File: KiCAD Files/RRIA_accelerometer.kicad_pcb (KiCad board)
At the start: 2 copper layers, 22 x 31.5 mm, 15 parts, among them J2 SPI LIS3DH, M1 Logo_Duet3d_New, U1 LIS3DH

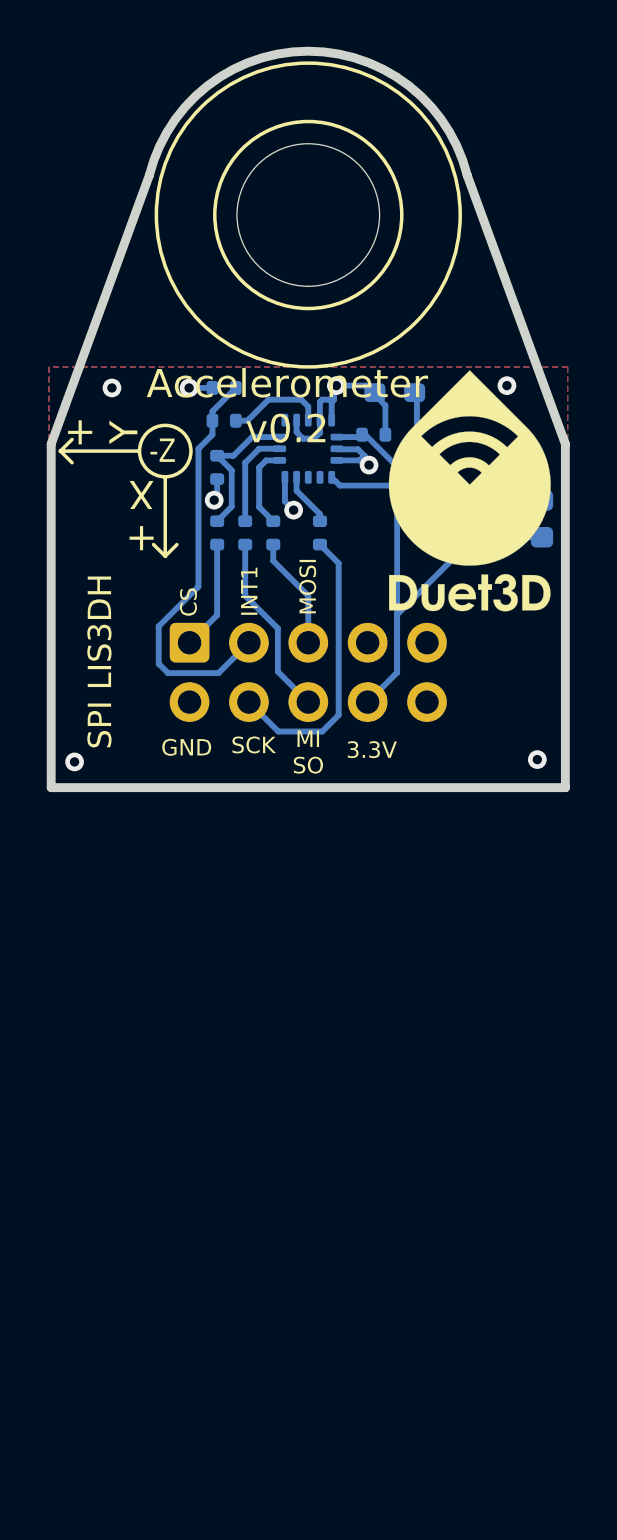
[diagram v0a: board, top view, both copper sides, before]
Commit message: gitignore + prep for RP2040
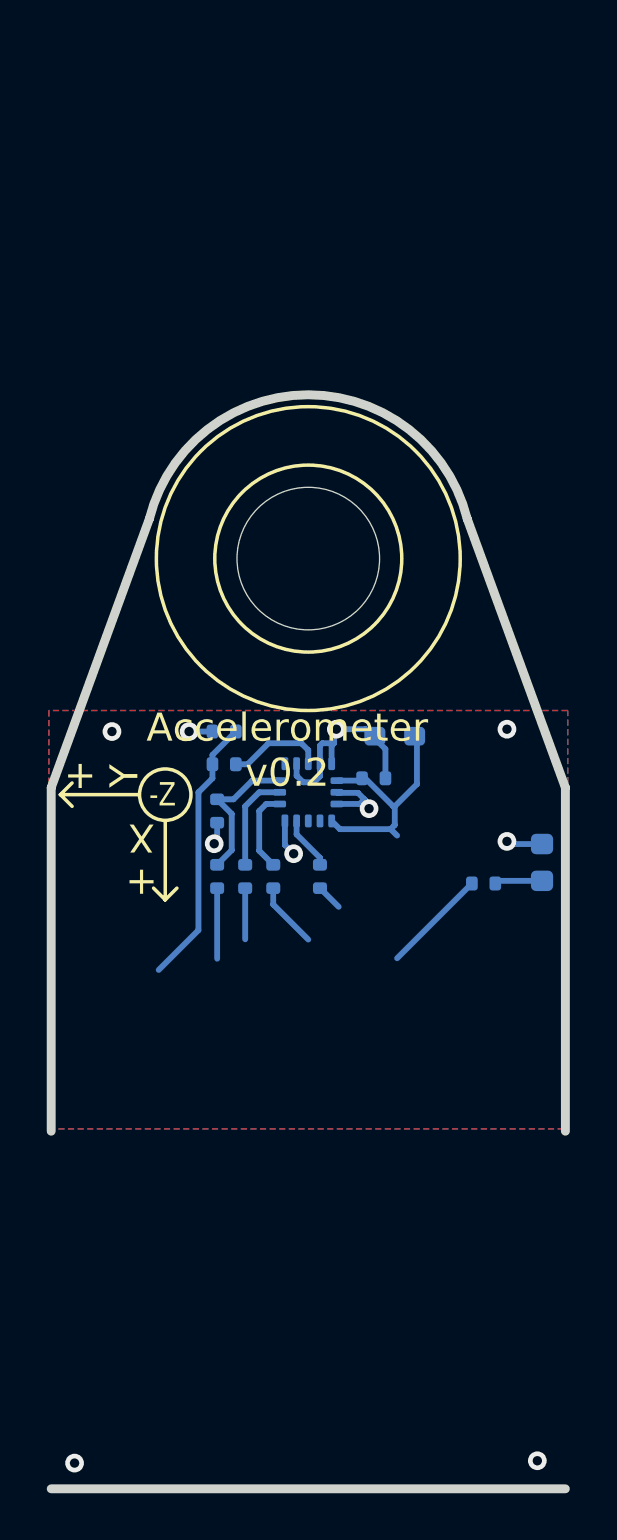
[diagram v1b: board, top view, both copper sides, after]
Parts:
- removed J2: SPI LIS3DH, Connector_IDC:IDC-Header_2x05_P2.54mm_Vertical
- removed M1: Logo_Duet3d_New, complib:LOGO_NEW_Duet3D_vertical_6mm_no_mask
- moved C1 14.7 mm to (73.8, 59.6)
- moved C3 14.7 mm to (67.1, 61.0)
- moved C4 14.7 mm to (67.4, 57.6)
- moved D1 14.7 mm to (81.0, 63.2)
- moved H1 14.7 mm to (71.0, 50.2)
- moved R1 14.7 mm to (67.4, 59.0)
- moved U1 14.7 mm to (71.0, 60.2)
- moved C2 14.7 mm to (74.7, 57.8)
- moved R2 14.7 mm to (68.3, 63.8)
- moved R3 14.7 mm to (69.5, 63.8)
- moved R4 14.7 mm to (71.5, 63.8)
- moved R5 14.7 mm to (67.1, 63.8)
- moved R6 14.7 mm to (78.5, 64.1)
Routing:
- net 3.3V: track 27.0 -> 15.0 mm
- net SPI_SCK: track 12.3 -> 1.13 mm
- net INT1: track 17.7 -> 11.6 mm
- net SPI_MISO: track 7.86 -> 2.19 mm
- net SPI_MOSI: track 4.82 -> 2.82 mm
- net SPI_CS: track 4.69 -> 3.02 mm
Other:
- board size 22 x 31.5 mm -> 22 x 46.8 mm
- board text removed: "3.3V"
- board text removed: "CS"
- board text removed: "GND"
- board text removed: "INT1"
- board text removed: "MI SO"
- board text removed: "MOSI"
- board text removed: "SCK"

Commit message: progress
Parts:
- removed D1: PWR, LED_SMD:LED_0603_1608Metric
- removed R1, R2, R3, R4, R5: 62R, Resistor_SMD:R_0402_1005Metric_Wbry
- removed R6: 220R, Resistor_SMD:R_0402_1005Metric_Wbry
- added C1: 100nF, Capacitor_SMD:C_0402_1005Metric, B.Cu at (163.4, 86.6)
- added C10: 100nF, Capacitor_SMD:C_0402_1005Metric, B.Cu at (161.3, 81.1)
- added C11: 1uF, Capacitor_SMD:C_0402_1005Metric, B.Cu at (177.2, 77.5)
- added C12: 1uF, Capacitor_SMD:C_0402_1005Metric, B.Cu at (169.4, 84.6)
- added C13: 10pF, Capacitor_SMD:C_0402_1005Metric, B.Cu at (162.7, 73.4)
- added C14: 10pF, Capacitor_SMD:C_0402_1005Metric, B.Cu at (166.6, 71.5)
- added C15: 100nF, Capacitor_SMD:C_0402_1005Metric, B.Cu at (165.0, 86.2)
- added C16: 100nF, Capacitor_SMD:C_0402_1005Metric, B.Cu at (169.3, 73.5)
- added C17: 8pF, Capacitor_SMD:C_0402_1005Metric, B.Cu at (145.7, 74.5)
- added C18: 8pF, Capacitor_SMD:C_0402_1005Metric, B.Cu at (146.0, 71.0)
- added C19: 100nF, Capacitor_SMD:C_0402_1005Metric, B.Cu at (150.9, 76.0)
- added C2: 100nF, Capacitor_SMD:C_0402_1005Metric, B.Cu at (161.4, 78.5)
- added C22: 1uF, Capacitor_SMD:C_0402_1005Metric, B.Cu at (150.9, 76.9)
- added C25: 100nF, Capacitor_SMD:C_0402_1005Metric, B.Cu at (132.6, 79.2)
- added C26: 100nF, Capacitor_SMD:C_0402_1005Metric, B.Cu at (132.6, 77.2)
- added C27: 1uF, Capacitor_SMD:C_0402_1005Metric, B.Cu at (132.6, 75.2)
- added C28: 1uF, Capacitor_SMD:C_0402_1005Metric, B.Cu at (132.6, 73.3)
- added C5: 100nF, Capacitor_SMD:C_0402_1005Metric, B.Cu at (168.4, 73.5)
- added C6: 1uF, Capacitor_SMD:C_0402_1005Metric, B.Cu at (168.5, 84.6)
- added C7: 100nF, Capacitor_SMD:C_0402_1005Metric, B.Cu at (171.5, 77.5)
- added C8: 100nF, Capacitor_SMD:C_0402_1005Metric, B.Cu at (165.9, 85.7)
- added C9: 100nF, Capacitor_SMD:C_0402_1005Metric, B.Cu at (166.8, 84.8)
- added J3: 2.54-Header-1x2, Connector_PinHeader_2.54mm:PinHeader_1x02_P2.54mm_Vertical, F.Cu at (185.6, 62.4)
- added R10: 1k, Resistor_SMD:R_0402_1005Metric, B.Cu at (166.6, 73.4)
- added R7: 120Ω, PCM_Resistor_SMD_AKL:R_0402_1005Metric, B.Cu at (130.7, 85.9)
- added SW1: TS-1088, Button_Switch_SMD:SW_SPST_TS-1088-xR025, B.Cu at (192.1, 62.0)
- added SW2: TS-1088, Button_Switch_SMD:SW_SPST_TS-1088-xR025, B.Cu at (192.1, 66.5)
- added U2: RP2040, Package_DFN_QFN:QFN-56-1EP_7x7mm_P0.4mm_EP3.2x3.2mm_ThermalVias, B.Cu at (166.4, 79.0)
- added U3: IS25WP016D, Package_SON:Winbond_USON-8-1EP_3x2mm_P0.5mm_EP0.2x1.6mm, B.Cu at (162.2, 84.8)
- added U4: MCP2518FD-xQBB, PCM_Package_DFN_QFN_AKL:DFN-14-1EP_3x4.5mm_P0.65mm_EP1.65x4.25mm, B.Cu at (149.6, 73.1)
- added U5: MCP2542FDxMF, PCM_Package_DFN_QFN_AKL:DFN-8-1EP_3x3mm_P0.65mm_EP1.7x2.05mm, B.Cu at (143.7, 78.9)
- added Y1: 12MHz, Crystal:Crystal_SMD_2520-4Pin_2.5x2.0mm, B.Cu at (164.6, 72.5)
- added Y2: 40MHz, Crystal:Crystal_SMD_2016-4Pin_2.0x1.6mm, B.Cu at (145.5, 72.8)
- C20: renamed from C1; value 0u1 6.3V -> 100nF; footprint Capacitor_SMD:C_0402_1005Metric_Wbry -> Capacitor_SMD:C_0402_1005Metric
- C21: renamed from C2; value 10u 10V -> 1uF; footprint Capacitor_SMD:C_0603_1608Metric_Wbry -> Capacitor_SMD:C_0402_1005Metric
- C3, C4: value 470p 6.3V -> 100nF; footprint Capacitor_SMD:C_0402_1005Metric_Wbry -> Capacitor_SMD:C_0402_1005Metric
- moved C4 106.7 mm to (171.5, 81.1), turned to -90 degrees
- moved C3 105.9 mm to (170.3, 84.6), turned to 90 degrees
- moved H1 86.7 mm to (156.4, 65.5)
- moved U1 86.7 mm to (156.4, 75.0), turned to -90 degrees
- moved C20 82.0 mm to (154.1, 76.3), turned to 90 degrees
- moved C21 80.9 mm to (154.1, 73.3), turned to -90 degrees
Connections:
- C20 pad 1: 3.3V -> GND
- C20 pad 2: GND -> +3V3
- C21 pad 1: 3.3V -> GND
- C21 pad 2: GND -> +3V3
- C3 pad 1: /cs -> GND
- C3 pad 2: GND -> +3V3
- C4 pad 1: INT1 -> GND
- C4 pad 2: GND -> +3V3
- U1 pad 1: 3.3V -> +3V3
- U1 pad 11: /int1 -> /INT1
- U1 pad 14: 3.3V -> +3V3
- U1 pad 4: /SCL -> SPI_SCK
- U1 pad 6: /SDI -> SPI_MOSI
- U1 pad 7: /SDO -> SPI_MISO
- U1 pad 8: /cs -> /CS_LIS
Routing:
- net +3V3: track 0.00 -> 29.9 mm
- net /MCP_INT: track 0.00 -> 21.3 mm, vias 0 -> 2
- net +1V1: track 0.00 -> 20.5 mm, vias 0 -> 4
- net SPI_SCK: track 1.13 -> 18.9 mm, vias 0 -> 3
- net /CS_CANFD: track 0.00 -> 16.6 mm, vias 0 -> 2
- net 3.3V: track 15.0 -> 0.00 mm
- net SPI_MOSI: track 2.82 -> 16.3 mm, vias 0 -> 2
- net SPI_MISO: track 2.19 -> 14.6 mm, vias 0 -> 2
- net INT1: track 11.6 -> 0.00 mm
- net GND: track 17.1 -> 6.38 mm, vias 10 -> 3
- net /QSPI-SS: track 0.00 -> 8.02 mm
- net /SD1: track 0.00 -> 7.38 mm
- net /INT1: track 0.00 -> 7.34 mm
- net /SD2: track 0.00 -> 6.74 mm
- net /cs: track 6.32 -> 0.00 mm
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- added copper zone on B.Cu, net +1V1
- added copper zone on B.Cu, net +3V3
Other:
- board size 22 x 46.8 mm -> 34 x 46.8 mm

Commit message: Final
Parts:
- added C23: 1uF, Capacitor_SMD:C_0402_1005Metric, B.Cu at (161.6, 96.1)
- added C24: 100nF, Capacitor_SMD:C_0402_1005Metric, B.Cu at (160.7, 96.1)
- added C29: 1uF, Capacitor_SMD:C_0402_1005Metric, B.Cu at (155.0, 95.2)
- added C30: 100nF, Capacitor_SMD:C_0402_1005Metric, B.Cu at (156.0, 95.2)
- added D1: GRN, PCM_LED_SMD_AKL:LED_0805_2012Metric, B.Cu at (154.9, 91.6)
- added D2: RED, PCM_LED_SMD_AKL:LED_0805_2012Metric, B.Cu at (160.6, 91.6)
- added J1: Conn_01x04, Connector_JST:JST_XH_S4B-XH-A_1x04_P2.50mm_Horizontal, B.Cu at (150.2, 91.0)
- added J2: USB_C_Receptacle_USB2.0_16P, CustomFootprints:USB_C_Receptacle_HRO_TYPE-C-31-M-12, B.Cu at (167.6, 96.6)
- added R1: 5.1kΩ, PCM_Resistor_SMD_AKL:R_0402_1005Metric, B.Cu at (169.9, 90.0)
- added R2: 5.1kΩ, PCM_Resistor_SMD_AKL:R_0402_1005Metric, B.Cu at (165.4, 90.0)
- added R3: 1kΩ, PCM_Resistor_SMD_AKL:R_0402_1005Metric, B.Cu at (154.8, 89.5)
- added R4: 1kΩ, PCM_Resistor_SMD_AKL:R_0402_1005Metric, B.Cu at (160.6, 89.5)
- added REF**: OSHW-Symbol_6.7x6mm_SilkScreen, Symbol:OSHW-Symbol_6.7x6mm_SilkScreen, F.Cu at (167.7, 93.2)
- added U6: TLV75733PDBV, PCM_Package_TO_SOT_SMD_AKL:SOT-23-5, B.Cu at (158.3, 97.0)
- added U7: USBLC6-2SC6, PCM_Package_TO_SOT_SMD_AKL:SOT-23-6, B.Cu at (167.6, 89.4)
- J3: moved to B.Cu
- moved J3 48.6 mm to (141.7, 83.5), turned to -90 degrees
- moved SW1 42.2 mm to (154.2, 80.6), turned to 0 degrees
- moved SW2 42.1 mm to (154.2, 84.9), turned to 0 degrees
- moved C11 17.8 mm to (159.9, 81.6), turned to 0 degrees
- moved C28 15.8 mm to (146.5, 80.8), turned to 90 degrees
- moved C26 13.5 mm to (145.6, 80.8), turned to 90 degrees
- moved C25 12.1 mm to (144.5, 77.0), turned to 180 degrees
- moved C27 11.9 mm to (144.5, 76.1), turned to 180 degrees
- moved R7 11.9 mm to (142.6, 85.7), turned to 180 degrees
- moved U5 0.82 mm to (143.3, 79.6)
- moved C13 0.74 mm to (162.7, 72.6)
- moved C14 0.74 mm to (166.6, 70.8)
- moved R10 0.74 mm to (166.6, 72.6)
- moved Y1 0.74 mm to (164.6, 71.8)
- moved C18 0.09 mm to (146.0, 70.9)
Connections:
- net Net-(J3-Pin_2) renamed /CANH
- net Net-(U5-CANH) renamed /CANL
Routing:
- net +3V3: track 29.9 -> 88.8 mm, vias 0 -> 2
- net +5V: track 0.00 -> 53.2 mm, vias 0 -> 3
- net /RUN: track 0.00 -> 24.9 mm, vias 0 -> 2
- net /CANL: track 0.00 -> 13.0 mm
- net /CANH: track 0.00 -> 11.7 mm
- net /CAN-TX: track 0.00 -> 8.09 mm, vias 0 -> 2
- net /CAN-RX: track 0.00 -> 6.86 mm
- net /QSPI-SS: track 8.02 -> 14.3 mm, vias 0 -> 2
- net GND: track 6.38 -> 11.5 mm, vias 3 -> 47
- net Net-(J2-D+-PadA6): track 0.00 -> 4.71 mm
- net Net-(J2-D--PadA7): track 0.00 -> 4.63 mm
- net Net-(J2-CC1): track 0.00 -> 2.49 mm
- net Net-(J2-CC2): track 0.00 -> 2.28 mm
- net /USB_D-: track 4.00 -> 5.98 mm
- net /USB_D+: track 4.01 -> 5.96 mm
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- added copper zone on B.Cu, net +5V
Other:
- board size 34 x 46.8 mm -> 34 x 41.2 mm
- board text added: "(ijo Pewa)"
- board text added: "+5V"
- board text added: "07MAR26"
- board text added: "3V3 POW"
- board text added: "BOOT"
- board text added: "Based on the design by Duet3D www.duet3d.com"
- board text added: "CAN TERM"
- board text added: "CAN-FD"
- board text added: "CANH"
- board text added: "CANL"
- board text added: "GND"
- board text added: "OHLv2-S"
- board text added: "OSHW"
- board text added: "RESET"
- board text added: "RepRap Integreated Accelerometer RRIA"
- board text added: "STATUS"
- board text added: "V0.1"
- board text added: "ijo[pilin=epiku=wawa=anpa=]"
- board text added: "transfur.science/f191"
- board text removed: "Accelerometer v0.2"
